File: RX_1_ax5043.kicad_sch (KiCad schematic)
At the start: 19 parts, among them J6 2118714-2, P5 CONUFL001-SMD-T, Q3 DMP2037U, U21 AX5043

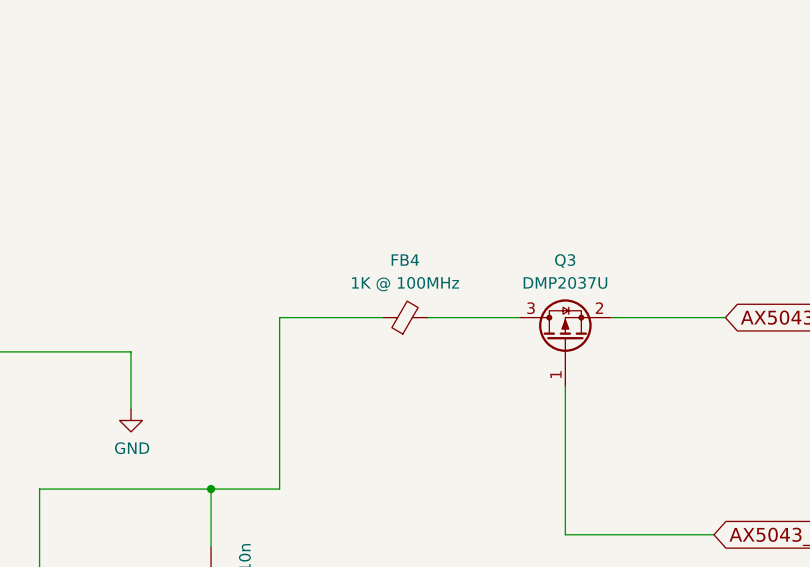
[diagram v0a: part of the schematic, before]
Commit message: More work on components
Signed-off-by: Corey Minyard <corey@minyard.net>
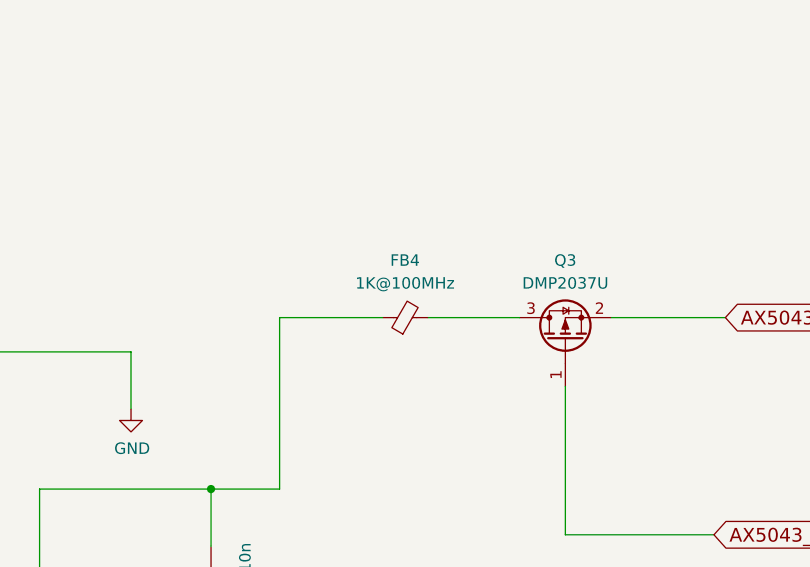
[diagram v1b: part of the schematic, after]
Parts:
- FB4: value 1K @ 100MHz -> 1K@100MHz
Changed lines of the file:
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@@
 			)
 		)
-		(property "Value" "1K @ 100MHz"
+		(property "Value" "1K@100MHz"
 			(at 266.6619 72.39 90)
 			(effects

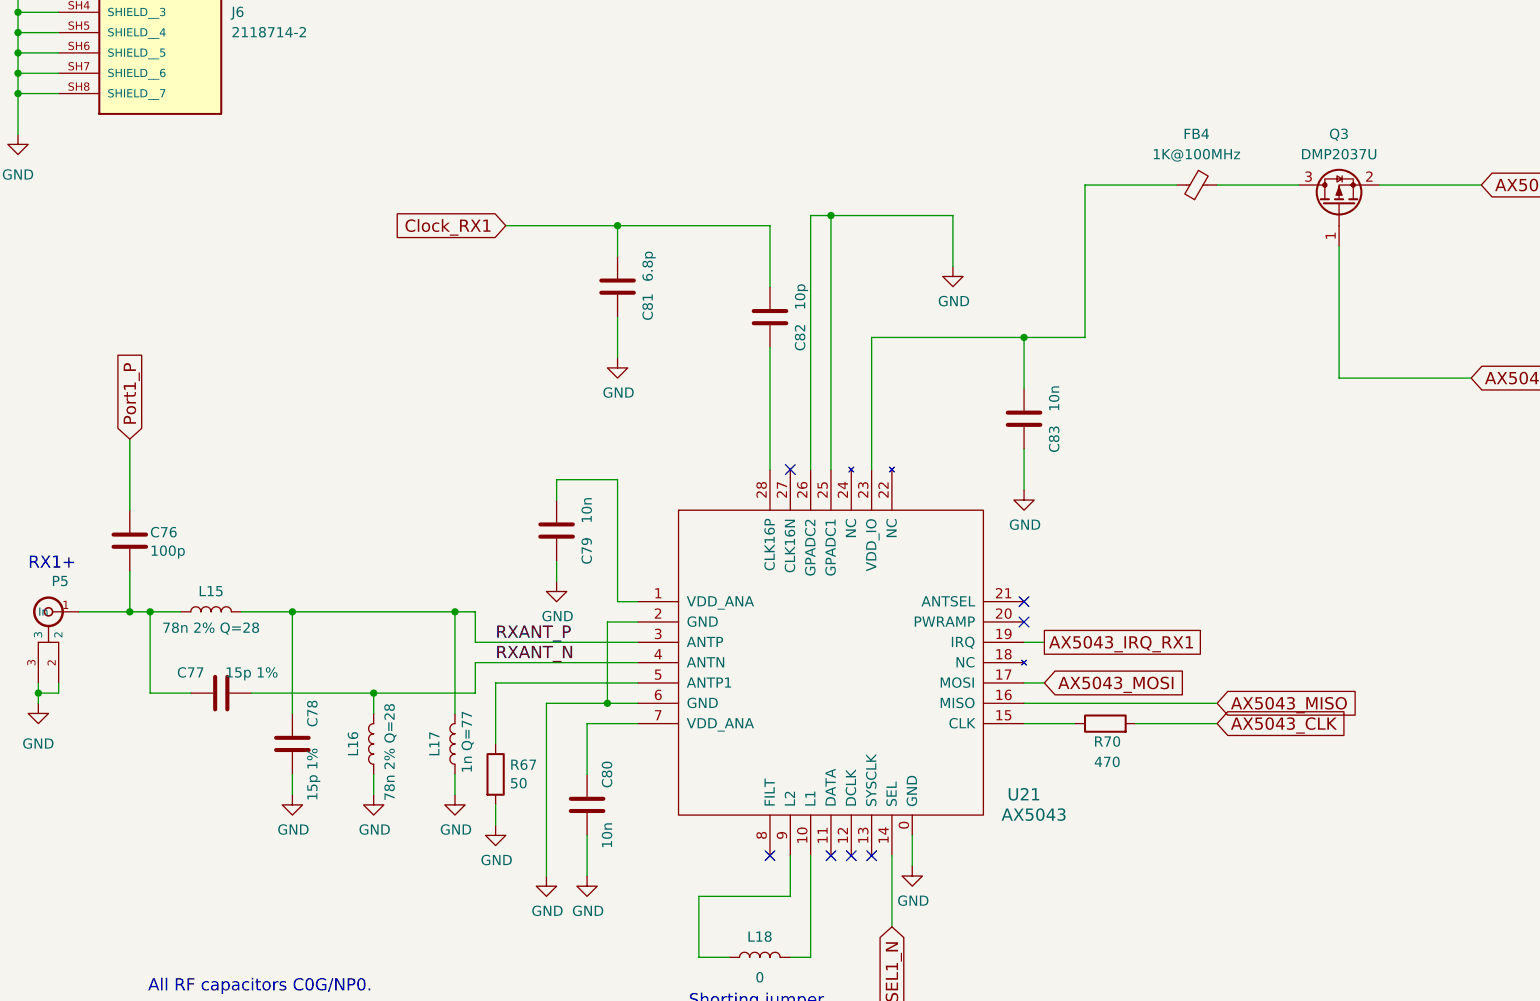
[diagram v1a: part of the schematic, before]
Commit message: Lots of updates to ease manufacturing
Component changes, changes in the formatting of the values, etc.

Signed-off-by: Corey Minyard <corey@minyard.net>
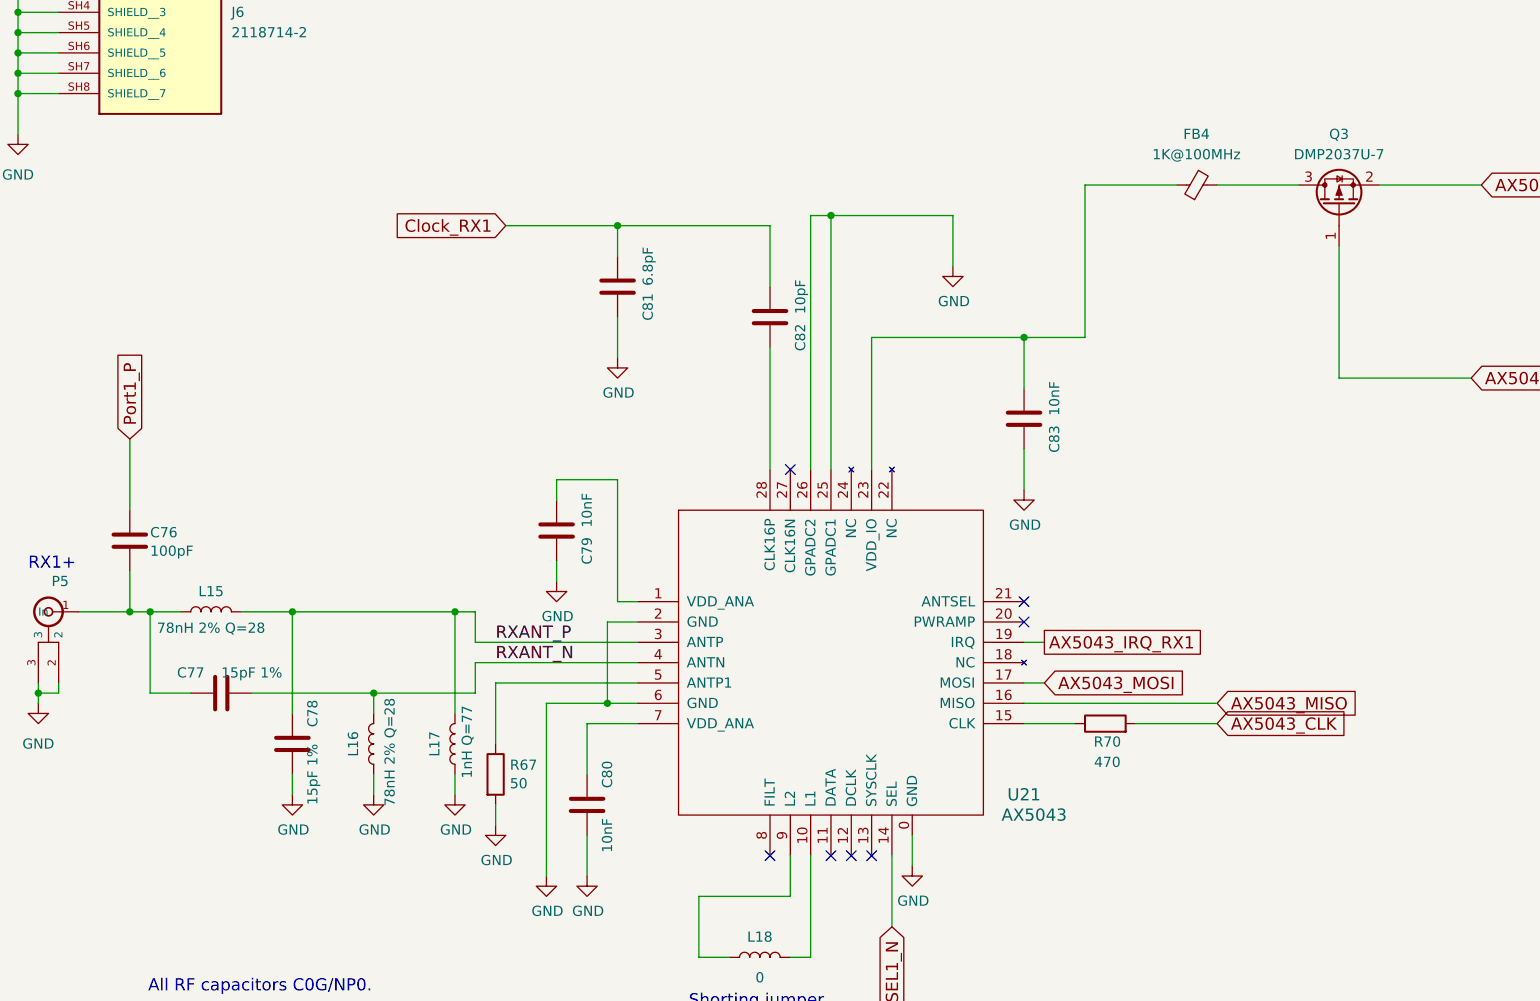
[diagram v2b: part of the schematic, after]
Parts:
- C76: value 100p -> 100pF
- C77, C78: value 15p 1% -> 15pF 1%
- C79, C80, C83: value 10n -> 10nF
- C81: value 6.8p -> 6.8pF
- C82: value 10p -> 10pF
- L15, L16: value 78n 2% Q=28 -> 78nH 2% Q=28
- L17: value 1n Q=77 -> 1nH Q=77
- Q3: value DMP2037U -> DMP2037U-7
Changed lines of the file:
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@@
 			)
 		)
-		(property "Value" "10n"
+		(property "Value" "10nF"
 			(at 193.04 157.48 90)
 			(effects
@@
 			)
 		)
-		(property "Value" "10p"
+		(property "Value" "10pF"
 			(at 217.17 90.17 90)
 			(effects
@@
 			)
 		)
-		(property "Value" "6.8p"
+		(property "Value" "6.8pF"
 			(at 198.12 86.36 90)
 			(effects
@@
 			)
 		)
-		(property "Value" "1n Q=77"
+		(property "Value" "1nH Q=77"
 			(at 175.514 145.796 90)
 			(effects
@@
 			)
 		)
-		(property "Value" "10n"
+		(property "Value" "10nF"
 			(at 248.92 102.87 90)
 			(effects
@@
 			)
 		)
-		(property "Value" "10n"
+		(property "Value" "10nF"
 			(at 190.5 116.84 90)
 			(effects
@@
 			)
 		)
-		(property "Value" "78n 2% Q=28"
+		(property "Value" "78nH 2% Q=28"
 			(at 143.51 131.572 90)
 			(effects
@@
 			)
 		)
-		(property "Value" "DMP2037U"
+		(property "Value" "DMP2037U-7"
 			(at 284.48 72.39 90)
 			(effects
@@
 			)
 		)
-		(property "Value" "78n 2% Q=28"
+		(property "Value" "78nH 2% Q=28"
 			(at 165.862 147.066 90)
 			(effects
@@
 			)
 		)
-		(property "Value" "100p"
+		(property "Value" "100pF"
 			(at 135.89 121.9454 0)
 			(effects
@@
 			)
 		)
-		(property "Value" "15p 1%"
+		(property "Value" "15pF 1%"
 			(at 148.59 137.16 90)
 			(effects
@@
 			)
 		)
-		(property "Value" "15p 1%"
+		(property "Value" "15pF 1%"
 			(at 156.21 149.86 90)
 			(effects

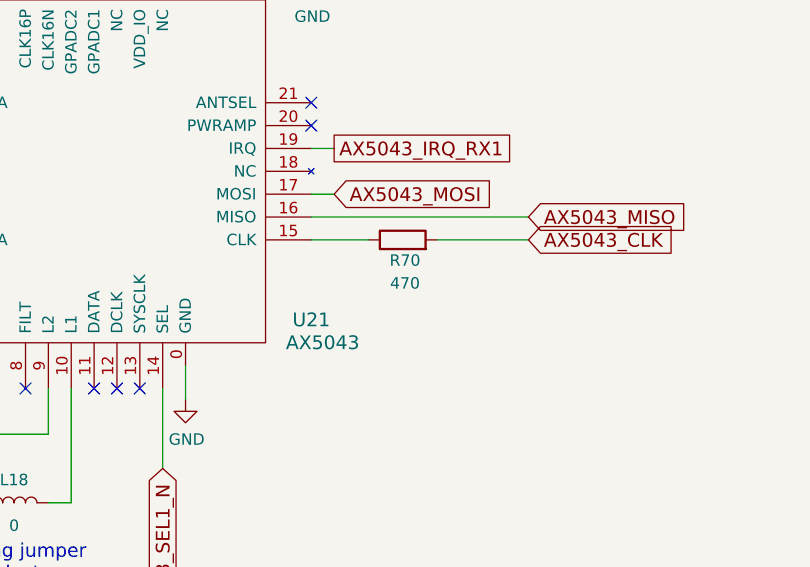
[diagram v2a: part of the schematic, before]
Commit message: Update all resistors to have an ohm symbol
Make it more clean in the BOM what they are.

Signed-off-by: Corey Minyard <corey@minyard.net>
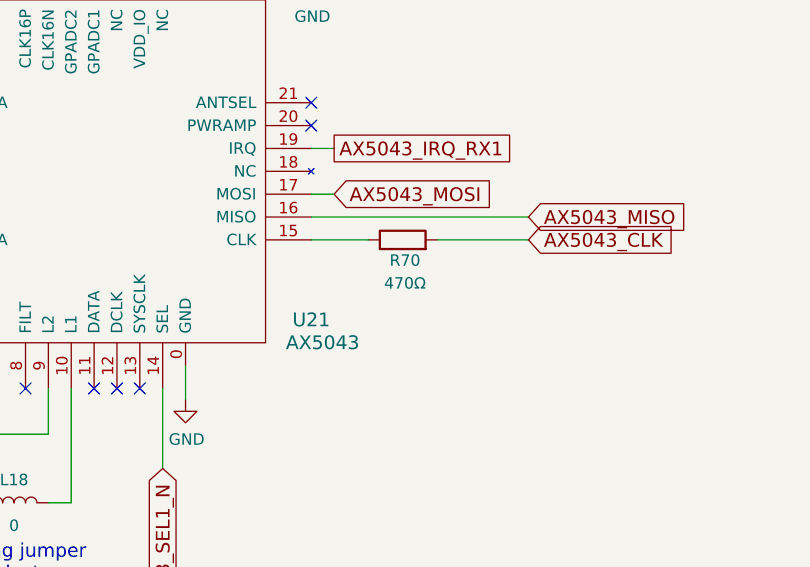
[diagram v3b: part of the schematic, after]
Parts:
- R70: value 470 -> 470Ω
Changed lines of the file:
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@@
 			)
 		)
-		(property "Value" "470"
+		(property "Value" "470Ω"
 			(at 255.524 148.336 90)
 			(effects

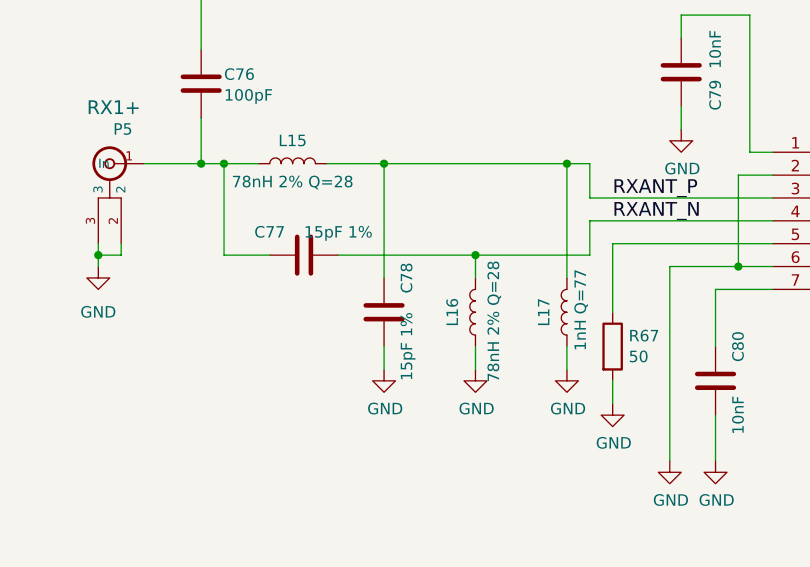
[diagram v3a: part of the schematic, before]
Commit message: Massive rework of filtering and inductors
Now that I know how inductors really work.

Signed-off-by: Corey Minyard <corey@minyard.net>
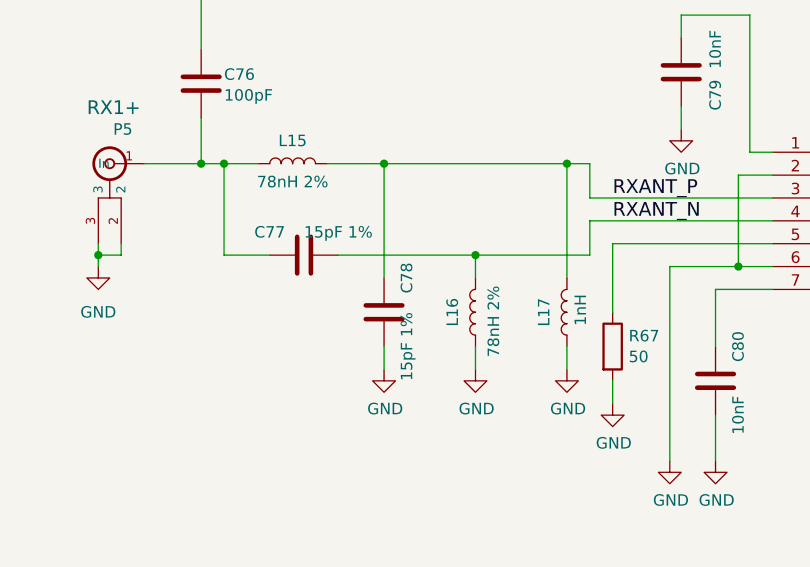
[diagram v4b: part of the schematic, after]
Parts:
- L15, L16: value 78nH 2% Q=28 -> 78nH 2%
- L17: value 1nH Q=77 -> 1nH
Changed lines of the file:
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@@
 			)
 		)
-		(property "Value" "1nH Q=77"
+		(property "Value" "1nH"
 			(at 175.514 145.796 90)
 			(effects
@@
 			)
 		)
-		(property "Value" "78nH 2% Q=28"
+		(property "Value" "78nH 2%"
 			(at 143.51 131.572 90)
 			(effects
@@
 			)
 		)
-		(property "Value" "78nH 2% Q=28"
+		(property "Value" "78nH 2%"
 			(at 165.862 147.066 90)
 			(effects

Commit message: Have the BOM file fixer output xls, not csv
The omega symbol gets translated properly from xls.

Signed-off-by: Corey Minyard <corey@minyard.net>
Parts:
- FB4: footprint Resistor_SMD:R_0603_1608Metric_Pad0.98x0.95mm_HandSolder -> Inductor_SMD:L_0603_1608Metric_Pad1.05x0.95mm_HandSolder
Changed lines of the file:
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@@
 			)
 		)
-		(property "Footprint" "Resistor_SMD:R_0603_1608Metric_Pad0.98x0.95mm_HandSolder"
+		(property "Footprint" "Inductor_SMD:L_0603_1608Metric_Pad1.05x0.95mm_HandSolder"
 			(at 266.7 77.978 90)
 			(effects

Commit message: Minor fixes for BOM values
Signed-off-by: Corey Minyard <corey@minyard.net>
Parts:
- FB4: value 1K@100MHz -> 1KΩ@100MHz
- R67: value 50 -> 50Ω
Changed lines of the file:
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@@
 			)
 		)
-		(property "Value" "1K@100MHz"
+		(property "Value" "1KΩ@100MHz"
 			(at 266.6619 72.39 90)
 			(effects
@@
 			)
 		)
-		(property "Value" "50"
+		(property "Value" "50Ω"
 			(at 180.848 151.003 0)
 			(effects

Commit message: A bunch of work on component selections
And little fixups for things I found.

Signed-off-by: Corey Minyard <corey@minyard.net>
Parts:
- C79: footprint Capacitor_SMD:C_0603_1608Metric_Pad1.08x0.95mm_HandSolder -> Capacitor_SMD:C_0402_1005Metric_Pad0.74x0.62mm_HandSolder
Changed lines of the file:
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@@
 			)
 		)
-		(property "Footprint" "Capacitor_SMD:C_0603_1608Metric_Pad1.08x0.95mm_HandSolder"
+		(property "Footprint" "Capacitor_SMD:C_0402_1005Metric_Pad0.74x0.62mm_HandSolder"
 			(at 187.6552 123.19 0)
 			(effects

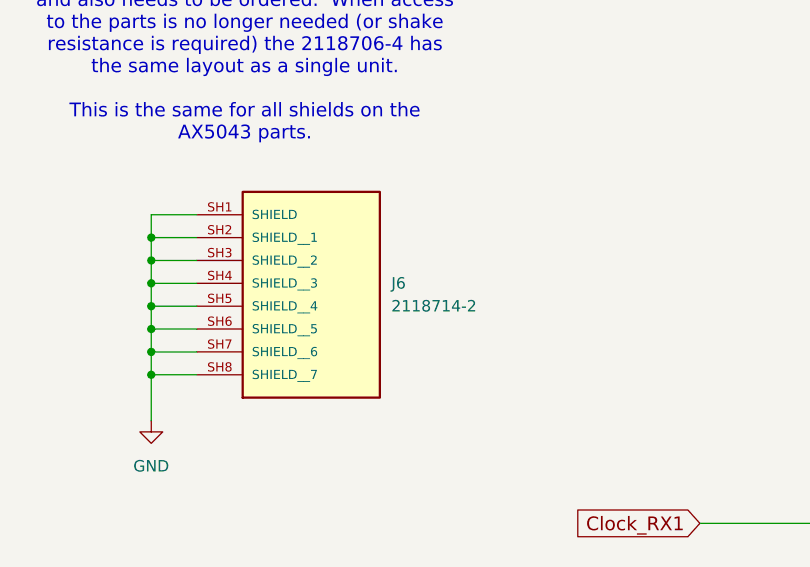
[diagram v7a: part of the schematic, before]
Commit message: Renumber shields and PC104 sockets
Separate out shields into their own designator category.

Make the PC104 sockets J1 and J2 to make it easier to move to other
boards.

Signed-off-by: Corey Minyard <corey@minyard.net>
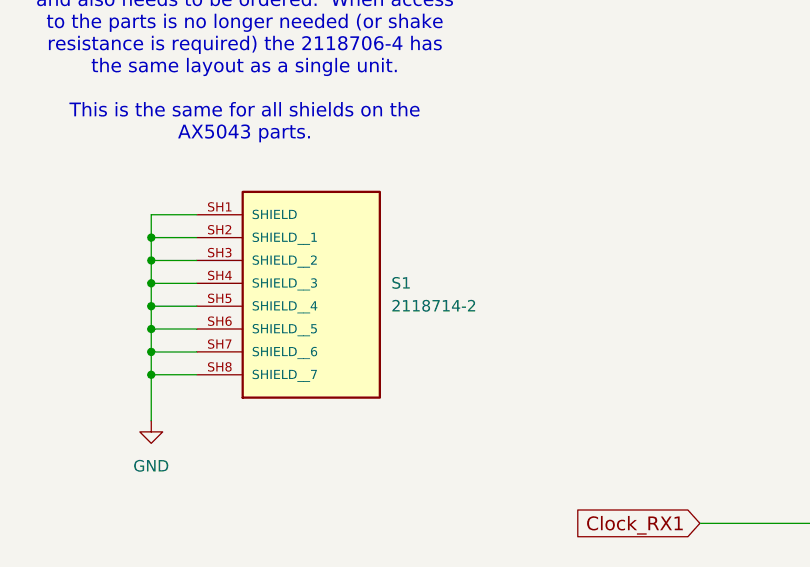
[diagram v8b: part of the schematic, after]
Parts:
- renumbered J6 to S1
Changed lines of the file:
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@@
 		(dnp no)
 		(fields_autoplaced yes)
-		(property "Reference" "J6"
+		(property "Reference" "S1"
 			(at 146.05 54.6099 0)
 			(effects
@@
 			(project "PacSat_AFSK"
 				(path "/cc9f42d2-6985-41ac-acab-5ab7b01c5b38/d9a83ee4-3280-49b9-88b8-54d26cbd8ed1/bc27fde3-8cca-4897-854d-674b6eeb65de"
-					(reference "J6")
+					(reference "S1")
 					(unit 1)
 				)
